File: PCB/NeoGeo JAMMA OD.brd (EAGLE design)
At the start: 63 x 38.5 mm, 20 parts, among them U1A ESP32DEVKITC, U2A SN74AHCT125N, U3A SN74AHCT125N, U4A SN74AHCT125N

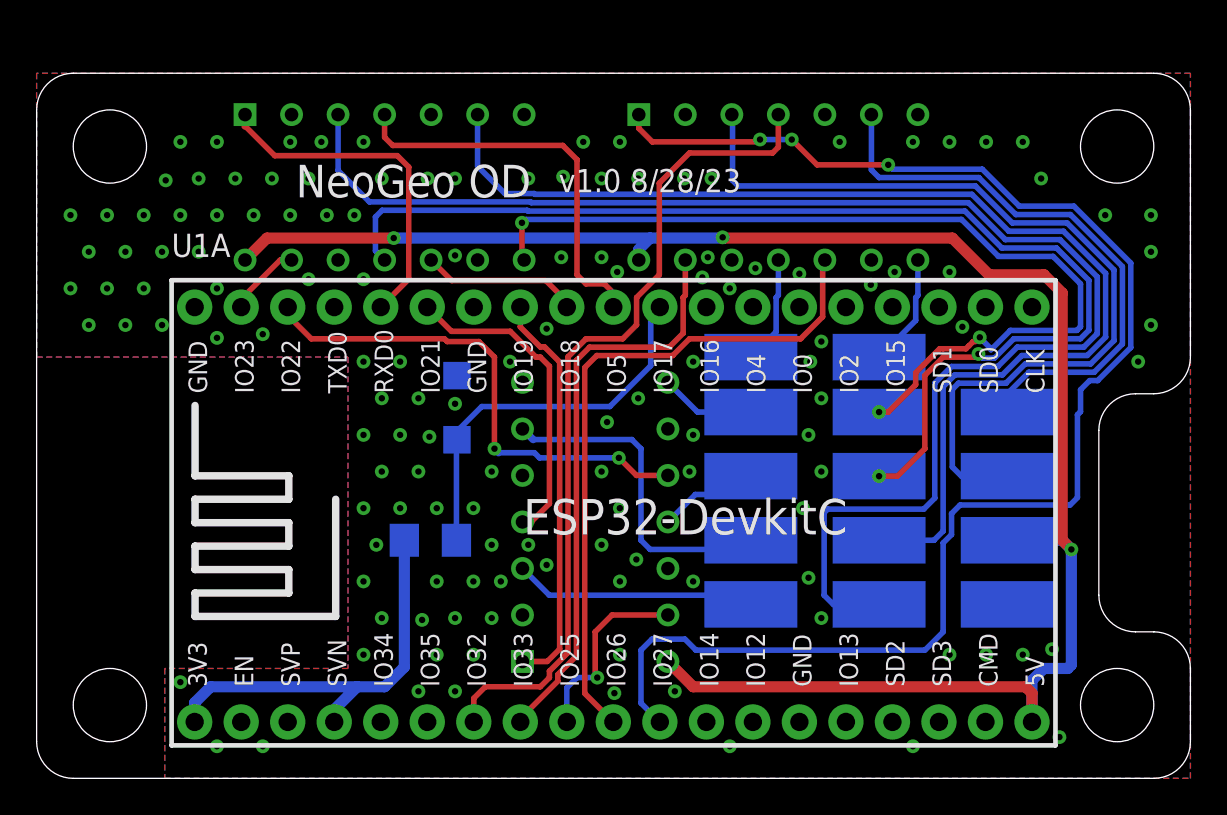
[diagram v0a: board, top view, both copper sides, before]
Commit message: ESP Size Change
The original design used an ESP with a 22mm spacing, Updated the part to the standard version with 25mm spacing.
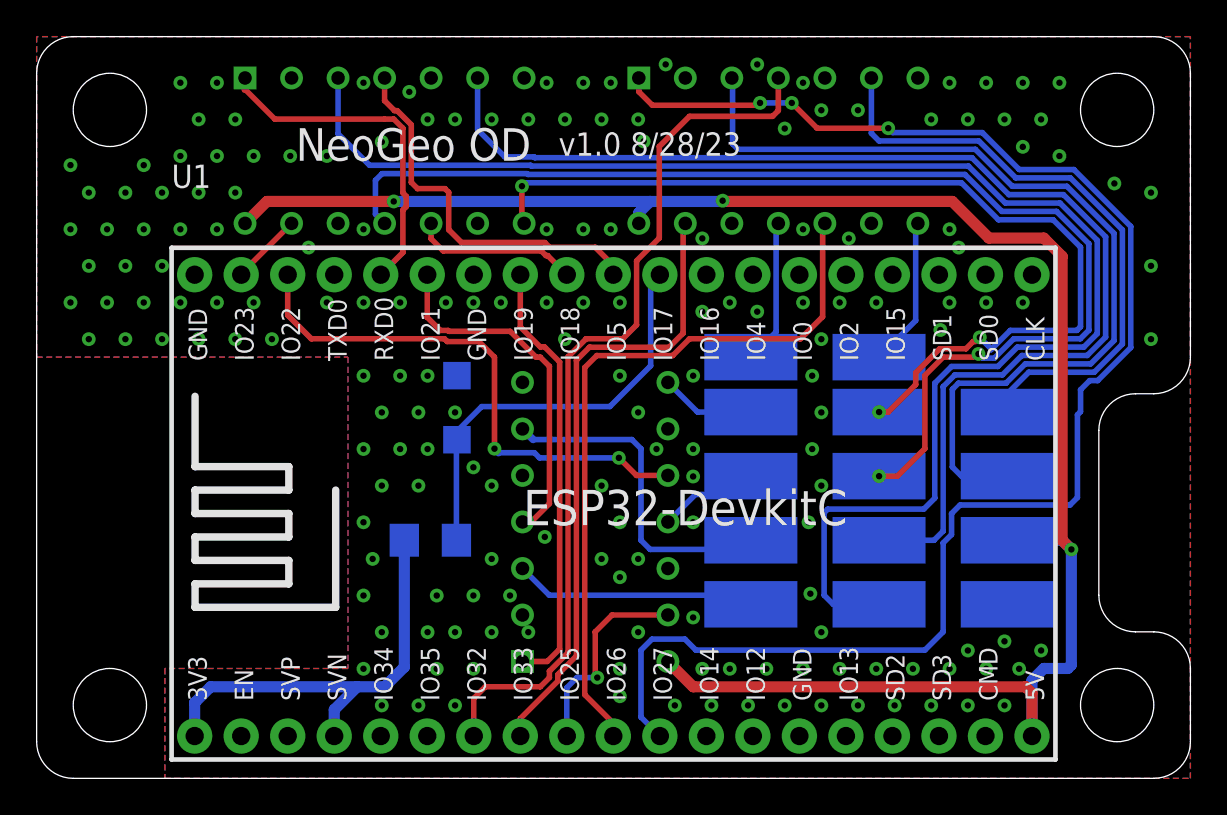
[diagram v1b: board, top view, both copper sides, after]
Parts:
- removed U1A: ESP32DEVKITC, ESP32-DEVKITC:ESP32-DEVKITC
- added U1: ESP32DEVKITC, ESP32-DEVKITC4:ESP32-DEVKITC
- moved U2A 2.00 mm to (40.5, 34.3)
- moved U3A 2.00 mm to (19.0, 34.3)
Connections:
- net 3V3IN: now also U1.1, U1.4; no longer U1A.1, U1A.4
- net 5VIN: now also U1.19; no longer U1A.19
- net GND: now also U1.38, U1.5, U1.6; no longer U1A.38, U1A.5, U1A.6
- net IO17: now also U1.28; no longer U1A.28
- net IO18: now also U1.30; no longer U1A.30
- net IO19: now also U1.31; no longer U1A.31
- net IO21: now also U1.33; no longer U1A.33
- net IO22: now also U1.36; no longer U1A.36
- net IO23: now also U1.37; no longer U1A.37
- net IO25: now also U1.9; no longer U1A.9
- net IO26: now also U1.10; no longer U1A.10
- net IO27: now also U1.11; no longer U1A.11
- net IO3: now also U1.34; no longer U1A.34
- net IO32: now also U1.7; no longer U1A.7
- net IO33: now also U1.8; no longer U1A.8
- net IO5: now also U1.29; no longer U1A.29
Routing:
- net 5VIN: track 99.0 -> 102.5 mm
- net IO32: track 45.6 -> 48.4 mm
- net IO33: track 31.5 -> 34.3 mm
- net IO27: track 80.7 -> 83.4 mm
- net IO26: track 37.3 -> 40.1 mm
- net IO21: track 17.4 -> 19.5 mm
- net U: track 80.4 -> 82.4 mm
- net START: track 31.6 -> 33.6 mm
- net L: track 50.4 -> 52.4 mm
- net DOWN: track 64.6 -> 66.6 mm
- net B: track 47.8 -> 49.8 mm
- net A: track 6.18 -> 8.18 mm
- net CREDIT: track 5.92 -> 7.92 mm
- net R: track 63.3 -> 65.3 mm
- net IO19: track 22.0 -> 23.8 mm
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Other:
- board size 63 x 38.5 mm -> 63 x 40.5 mm
